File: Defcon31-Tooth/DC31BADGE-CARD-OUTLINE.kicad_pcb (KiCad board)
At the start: 2 copper layers, 42.8 x 68.9 mm, 7 parts

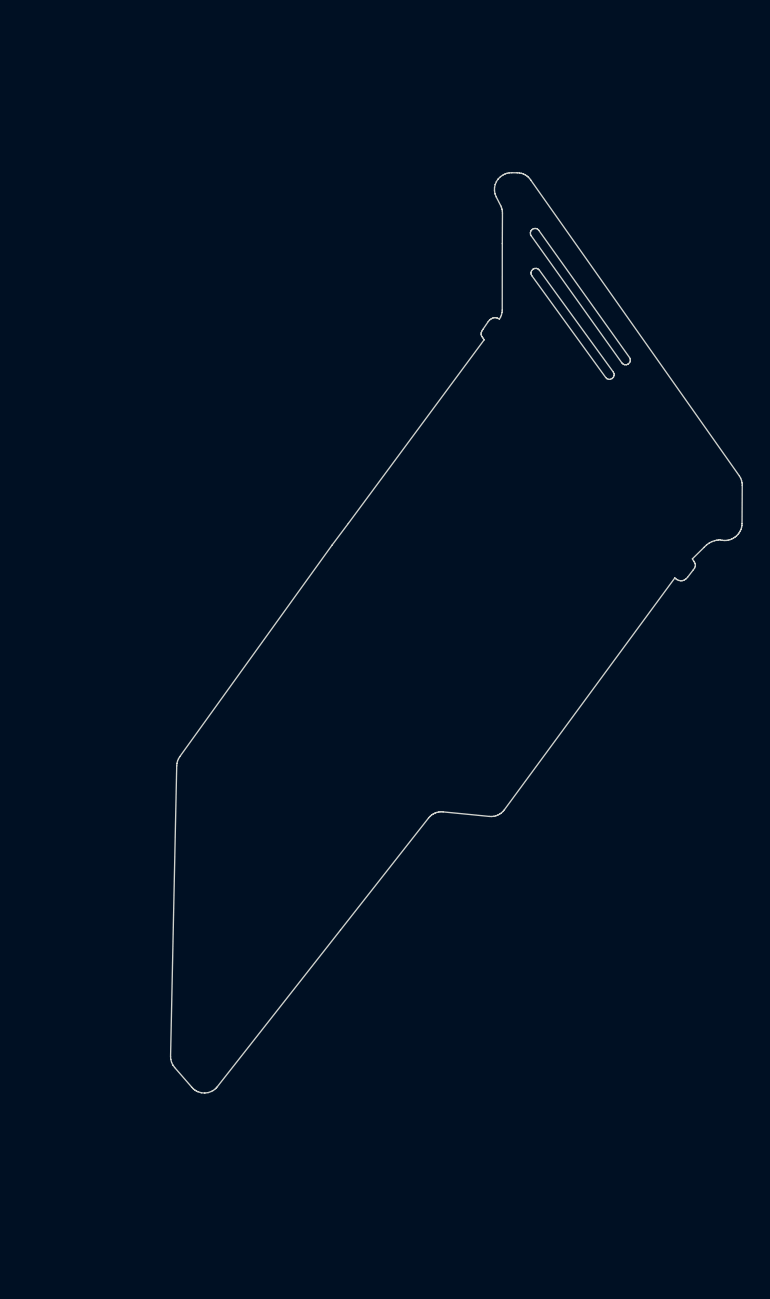
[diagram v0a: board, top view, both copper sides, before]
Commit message: Fixed dimentions to account for error between Adobe and Inkscape
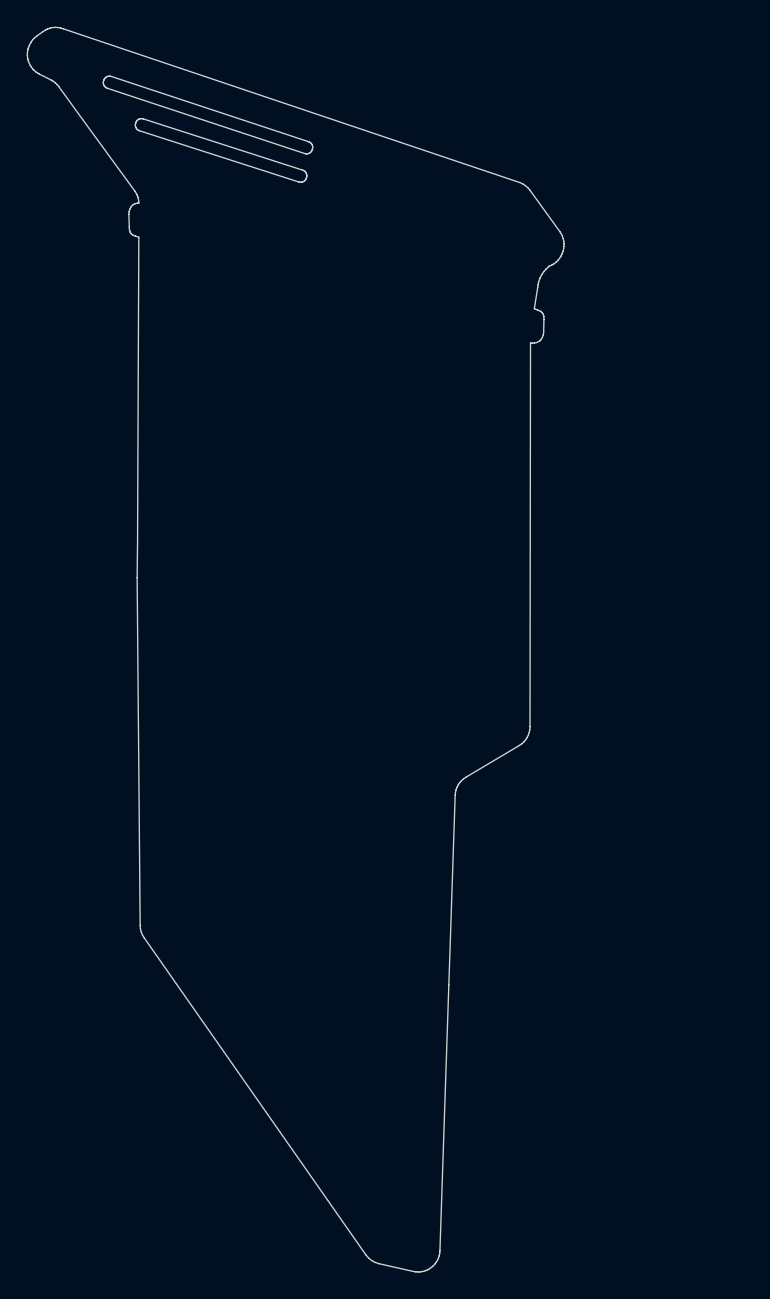
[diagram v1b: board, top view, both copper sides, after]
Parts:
- removed the G*** at (161.5, 96.7) (x7)
- added G*** (x7): LOGO, LOGO, F.Cu at (150.8, 96.4)
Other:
- board size 42.8 x 68.9 mm -> 40.2 x 93.2 mm
